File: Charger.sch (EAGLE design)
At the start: 15 parts, among them Q1 SPP80P06P

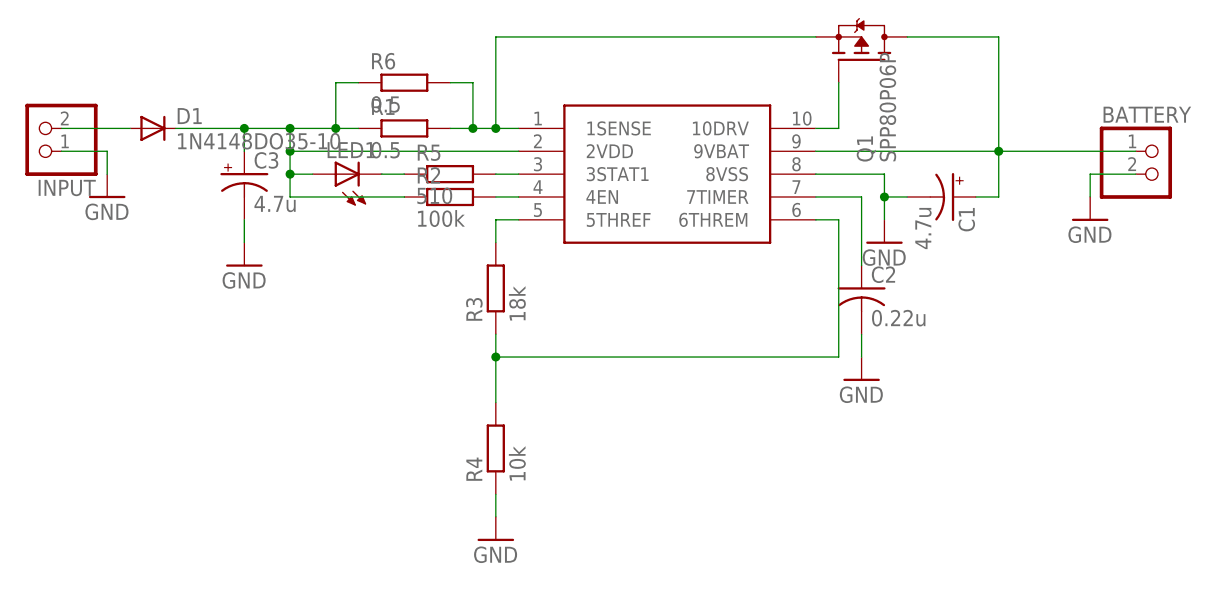
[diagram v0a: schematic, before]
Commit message: Revert "Add values of capacitors and parallel resistors"
This reverts commit c5449c38890c53df2ecf398a39eaa116fb527d7b.
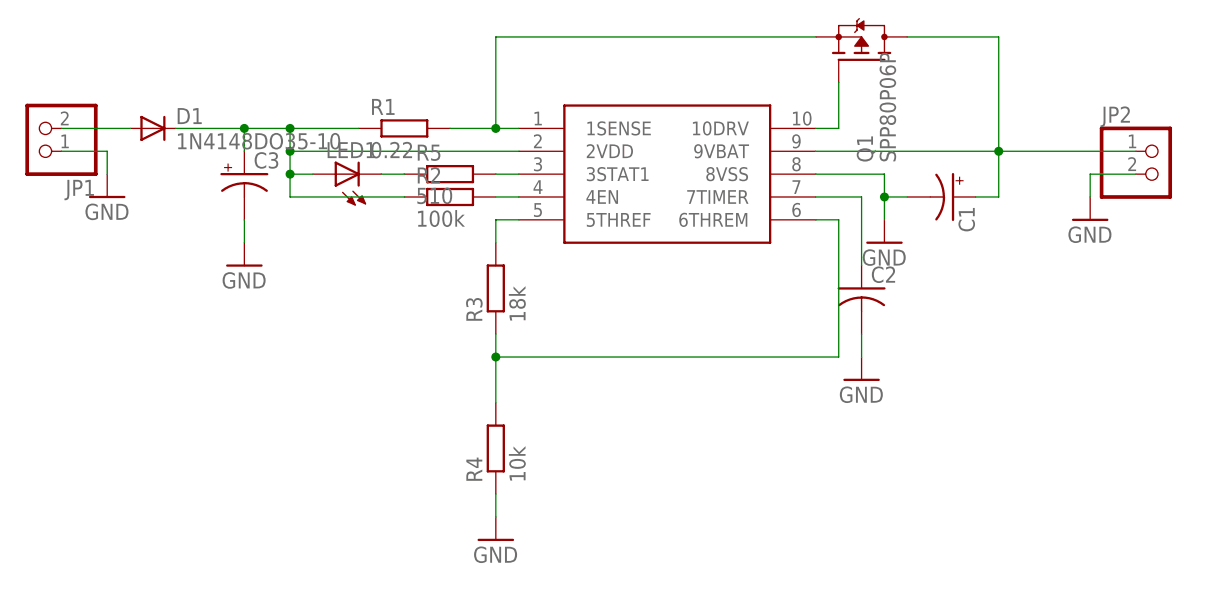
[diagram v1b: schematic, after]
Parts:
- removed R6: 0.5, resistor:R-EU_R0805
- C1, C3: value 4.7u -> (none)
- C2: value 0.22u -> (none)
- R1: value 0.5 -> 0.22
- renumbered BATTERY to JP2, INPUT to JP1
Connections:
- net N$1: no longer R6.1
- net N$2: no longer R6.2
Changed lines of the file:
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@@
 <part name="U$1" library="mcp73841" deviceset="MCP73841" device=""/>
 <part name="D1" library="diode" deviceset="1N4148" device="DO35-10"/>
-<part name="R1" library="resistor" deviceset="R-EU_" device="R0805" value="0.5"/>
+<part name="R1" library="resistor" deviceset="R-EU_" device="R0805" value="0.22"/>
 <part name="R2" library="resistor" deviceset="R-EU_" device="R0805" value="100k"/>
 <part name="LED1" library="led" deviceset="LED" device="CHIPLED_1206"/>
 <part name="Q1" library="transistor-fet" deviceset="SPP80P06P" device=""/>
-<part name="C1" library="resistor" deviceset="CPOL-US" device="153CLV-0505" value="4.7u"/>
-<part name="C2" library="resistor" deviceset="C-US" device="C0805" value="0.22u"/>
+<part name="C1" library="resistor" deviceset="CPOL-US" device="153CLV-0505"/>
+<part name="C2" library="resistor" deviceset="C-US" device="C0805"/>
 <part name="GND1" library="supply1" deviceset="GND" device=""/>
 <part name="GND2" library="supply1" deviceset="GND" device=""/>
-<part name="C3" library="resistor" deviceset="CPOL-US" device="153CLV-0505" value="4.7u"/>
+<part name="C3" library="resistor" deviceset="CPOL-US" device="153CLV-0505"/>
 <part name="GND3" library="supply1" deviceset="GND" device=""/>
 <part name="R3" library="resistor" deviceset="R-EU_" device="R0805" value="18k"/>
@@
 <part name="GND4" library="supply1" deviceset="GND" device=""/>
 <part name="R5" library="resistor" deviceset="R-EU_" device="R0805" value="510"/>
-<part name="INPUT" library="pinhead" deviceset="PINHD-1X2" device=""/>
-<part name="BATTERY" library="pinhead" deviceset="PINHD-1X2" device=""/>
+<part name="JP1" library="pinhead" deviceset="PINHD-1X2" device=""/>
+<part name="JP2" library="pinhead" deviceset="PINHD-1X2" device=""/>
 <part name="GND5" library="supply1" deviceset="GND" device=""/>
 <part name="GND6" library="supply1" deviceset="GND" device=""/>
-<part name="R6" library="resistor" deviceset="R-EU_" device="R0805" value="0.5"/>
 </parts>
 <sheets>
@@
 <instance part="GND4" gate="1" x="-20.32" y="-40.64"/>
 <instance part="R5" gate="G$1" x="-25.4" y="0"/>
-<instance part="INPUT" gate="G$1" x="-71.12" y="5.08" rot="R180"/>
-<instance part="BATTERY" gate="G$1" x="53.34" y="0"/>
+<instance part="JP1" gate="G$1" x="-71.12" y="5.08" rot="R180"/>
+<instance part="JP2" gate="G$1" x="53.34" y="0"/>
 <instance part="GND5" gate="1" x="45.72" y="-5.08"/>
 <instance part="GND6" gate="1" x="-63.5" y="-2.54"/>
-<instance part="R6" gate="G$1" x="-30.48" y="10.16"/>
 </instances>
 <busses>
@@
 <pinref part="U$1" gate="G$1" pin="2VDD"/>
 <wire x1="-48.26" y1="5.08" x2="-43.18" y2="5.08" width="0.1524" layer="91"/>
-<wire x1="-43.18" y1="5.08" x2="-38.1" y2="5.08" width="0.1524" layer="91"/>
-<wire x1="-38.1" y1="5.08" x2="-35.56" y2="5.08" width="0.1524" layer="91"/>
+<wire x1="-43.18" y1="5.08" x2="-35.56" y2="5.08" width="0.1524" layer="91"/>
 <wire x1="-17.78" y1="2.54" x2="-43.18" y2="2.54" width="0.1524" layer="91"/>
 <wire x1="-43.18" y1="2.54" x2="-43.18" y2="5.08" width="0.1524" layer="91"/>
@@
 <wire x1="-48.26" y1="5.08" x2="-48.26" y2="2.54" width="0.1524" layer="91"/>
 <junction x="-48.26" y="5.08"/>
-<pinref part="R6" gate="G$1" pin="1"/>
-<wire x1="-35.56" y1="10.16" x2="-38.1" y2="10.16" width="0.1524" layer="91"/>
-<wire x1="-38.1" y1="10.16" x2="-38.1" y2="5.08" width="0.1524" layer="91"/>
-<junction x="-38.1" y="5.08"/>
 </segment>
 </net>
@@
 <pinref part="R1" gate="G$1" pin="2"/>
 <pinref part="U$1" gate="G$1" pin="1SENSE"/>
-<wire x1="-25.4" y1="5.08" x2="-22.86" y2="5.08" width="0.1524" layer="91"/>
+<wire x1="-25.4" y1="5.08" x2="-20.32" y2="5.08" width="0.1524" layer="91"/>
 <pinref part="Q1" gate="G$1" pin="S"/>
-<wire x1="-22.86" y1="5.08" x2="-20.32" y2="5.08" width="0.1524" layer="91"/>
 <wire x1="-20.32" y1="5.08" x2="-17.78" y2="5.08" width="0.1524" layer="91"/>
 <wire x1="15.24" y1="15.24" x2="-20.32" y2="15.24" width="0.1524" layer="91"/>
 <wire x1="-20.32" y1="15.24" x2="-20.32" y2="5.08" width="0.1524" layer="91"/>
 <junction x="-20.32" y="5.08"/>
-<pinref part="R6" gate="G$1" pin="2"/>
-<wire x1="-25.4" y1="10.16" x2="-22.86" y2="10.16" width="0.1524" layer="91"/>
-<wire x1="-22.86" y1="10.16" x2="-22.86" y2="5.08" width="0.1524" layer="91"/>
-<junction x="-22.86" y="5.08"/>
 </segment>
 </net>
@@
 <wire x1="35.56" y1="-2.54" x2="35.56" y2="2.54" width="0.1524" layer="91"/>
 <junction x="35.56" y="2.54"/>
-<pinref part="BATTERY" gate="G$1" pin="1"/>
+<pinref part="JP2" gate="G$1" pin="1"/>
 <wire x1="50.8" y1="2.54" x2="35.56" y2="2.54" width="0.1524" layer="91"/>
 </segment>
@@
 </segment>
 <segment>
-<pinref part="BATTERY" gate="G$1" pin="2"/>
+<pinref part="JP2" gate="G$1" pin="2"/>
 <wire x1="50.8" y1="0" x2="45.72" y2="0" width="0.1524" layer="91"/>
 <wire x1="45.72" y1="0" x2="45.72" y2="-2.54" width="0.1524" layer="91"/>
@@
 </segment>
 <segment>
-<pinref part="INPUT" gate="G$1" pin="1"/>
+<pinref part="JP1" gate="G$1" pin="1"/>
 <wire x1="-68.58" y1="2.54" x2="-63.5" y2="2.54" width="0.1524" layer="91"/>
 <wire x1="-63.5" y1="2.54" x2="-63.5" y2="0" width="0.1524" layer="91"/>
@@
 <net name="N$10" class="0">
 <segment>
-<pinref part="INPUT" gate="G$1" pin="2"/>
+<pinref part="JP1" gate="G$1" pin="2"/>
 <pinref part="D1" gate="G$1" pin="A"/>
 <wire x1="-68.58" y1="5.08" x2="-60.96" y2="5.08" width="0.1524" layer="91"/>
